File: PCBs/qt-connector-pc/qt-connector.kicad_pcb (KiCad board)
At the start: 2 copper layers, 40.9 x 53 mm, 6 parts, among them J1 DE9_Plug_MountingHoles, K2 Modem port, K3 Printer port, K4 ImageWriter

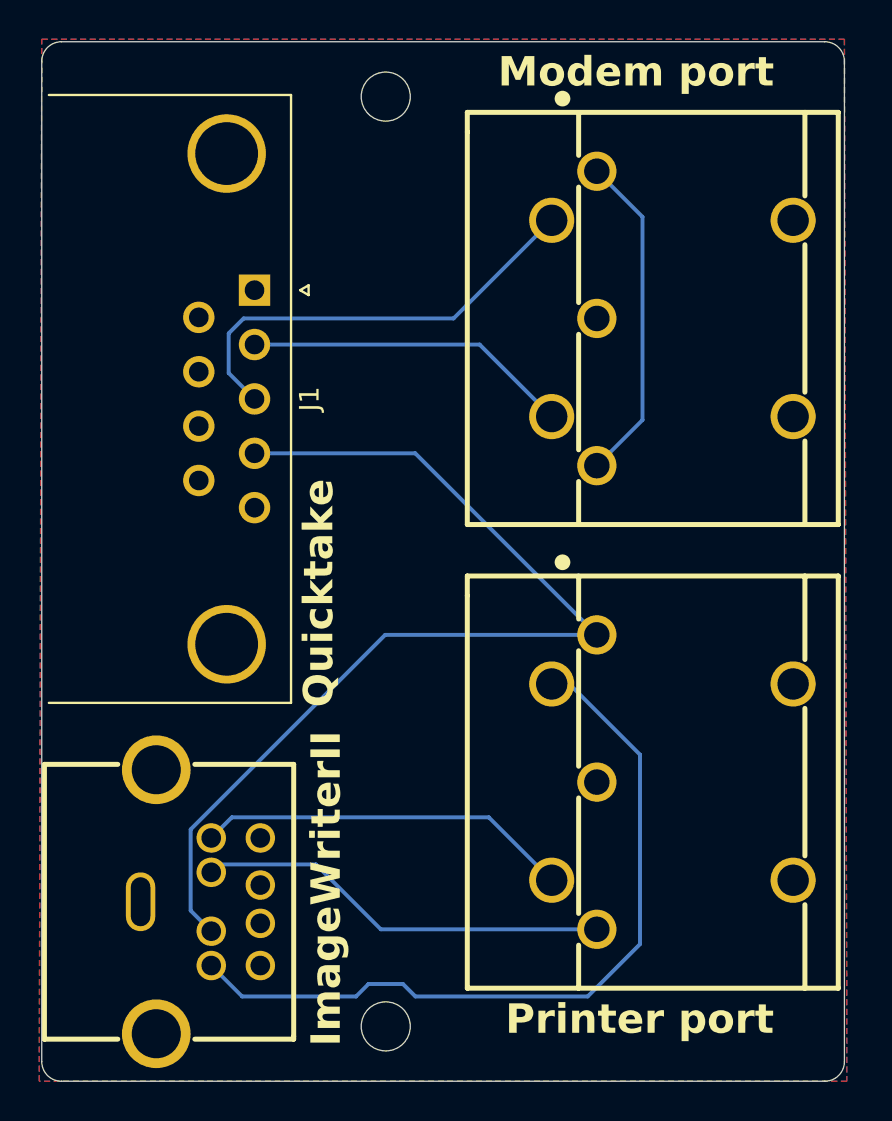
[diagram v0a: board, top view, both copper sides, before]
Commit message: Fixes (mounting holes!) and more adapters
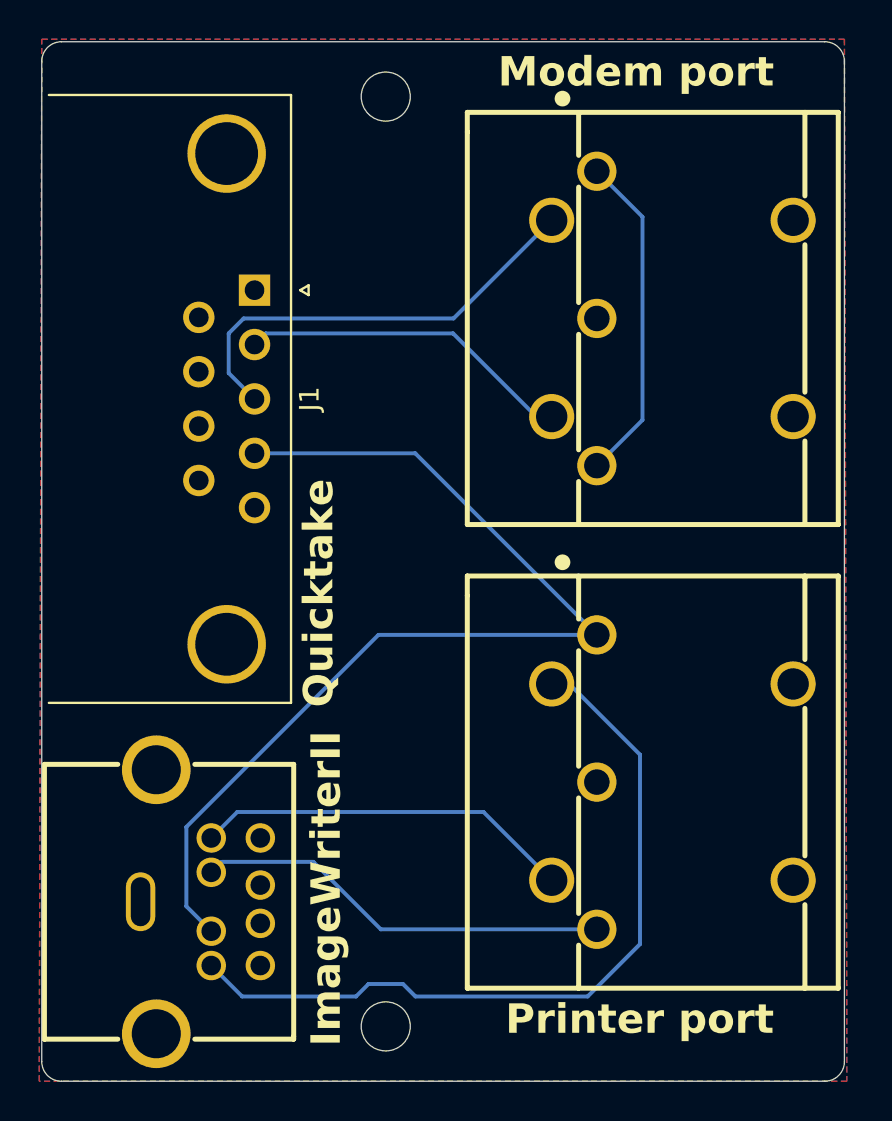
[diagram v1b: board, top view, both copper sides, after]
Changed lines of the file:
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@@
 	)
 	(segment
-		(start 137.627 89.468)
+		(start 136.271 88.9)
+		(end 126.725 88.9)
+		(width 0.2)
+		(layer "B.Cu")
+		(net 6)
+	)
+	(segment
+		(start 141.297 93.138)
+		(end 140.509 93.138)
+		(width 0.2)
+		(layer "B.Cu")
+		(net 6)
+	)
+	(segment
+		(start 126.725 88.9)
 		(end 126.157 89.468)
 		(width 0.2)
@@
 	)
 	(segment
-		(start 141.297 93.138)
-		(end 137.627 89.468)
+		(start 140.509 93.138)
+		(end 136.271 88.9)
 		(width 0.2)
 		(layer "B.Cu")
@@
 	)
 	(segment
-		(start 138.092 113.555)
+		(start 125.274 113.284)
+		(end 137.821 113.284)
+		(width 0.2)
+		(layer "B.Cu")
+		(net 9)
+	)
+	(segment
+		(start 123.952 114.606)
+		(end 125.274 113.284)
+		(width 0.2)
+		(layer "B.Cu")
+		(net 9)
+	)
+	(segment
+		(start 137.821 113.284)
 		(end 141.297 116.76)
-		(width 0.2)
-		(layer "B.Cu")
-		(net 9)
-	)
-	(segment
-		(start 123.952 114.606)
-		(end 125.003 113.555)
-		(width 0.2)
-		(layer "B.Cu")
-		(net 9)
-	)
-	(segment
-		(start 125.003 113.555)
-		(end 138.092 113.555)
 		(width 0.2)
 		(layer "B.Cu")
@@
 	)
 	(segment
-		(start 124.353 115.955)
-		(end 129.287339 115.955)
-		(width 0.2)
-		(layer "B.Cu")
-		(net 11)
-	)
-	(segment
-		(start 123.952 116.356)
-		(end 124.353 115.955)
-		(width 0.2)
-		(layer "B.Cu")
-		(net 11)
-	)
-	(segment
-		(start 129.287339 115.955)
-		(end 132.592339 119.26)
+		(start 124.484 115.824)
+		(end 129.156339 115.824)
 		(width 0.2)
 		(layer "B.Cu")
@@
 	)
 	(segment
+		(start 129.156339 115.824)
+		(end 132.592339 119.26)
+		(width 0.2)
+		(layer "B.Cu")
+		(net 11)
+	)
+	(segment
+		(start 123.952 116.356)
+		(end 124.484 115.824)
+		(width 0.2)
+		(layer "B.Cu")
+		(net 11)
+	)
+	(segment
+		(start 132.468 104.26)
+		(end 143.597 104.26)
+		(width 0.2)
+		(layer "B.Cu")
+		(net 14)
+	)
+	(segment
+		(start 123.952 119.356)
+		(end 122.682 118.086)
+		(width 0.2)
+		(layer "B.Cu")
+		(net 14)
+	)
+	(segment
+		(start 122.682 114.046)
+		(end 132.468 104.26)
+		(width 0.2)
+		(layer "B.Cu")
+		(net 14)
+	)
+	(segment
 		(start 143.597 104.26)
 		(end 134.345 95.008)
@@
 	)
 	(segment
-		(start 132.811661 104.26)
-		(end 143.597 104.26)
-		(width 0.2)
-		(layer "B.Cu")
-		(net 14)
-	)
-	(segment
-		(start 123.952 119.356)
-		(end 122.901 118.305)
-		(width 0.2)
-		(layer "B.Cu")
-		(net 14)
-	)
-	(segment
-		(start 122.901 118.305)
-		(end 122.901 114.170661)
-		(width 0.2)
-		(layer "B.Cu")
-		(net 14)
-	)
-	(segment
-		(start 122.901 114.170661)
-		(end 132.811661 104.26)
-		(width 0.2)
-		(layer "B.Cu")
+		(start 122.682 118.086)
+		(end 122.682 114.046)
+		(width 0.2)
+		(layer "B.Cu")
